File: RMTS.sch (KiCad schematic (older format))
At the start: 68 parts, among them J1 USB_B_Mini, J10 CONN_02, J2 Programmer, J3 Screw_Terminal_01x03, J4 Screw_Terminal_01x04, J5 Screw_Terminal_01x02, J6 Screw_Terminal_01x02, J7 Micro_SD_Card_Det_Hirose_DM3AT, J8 Screw_Terminal_01x02, J9 CONN_02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

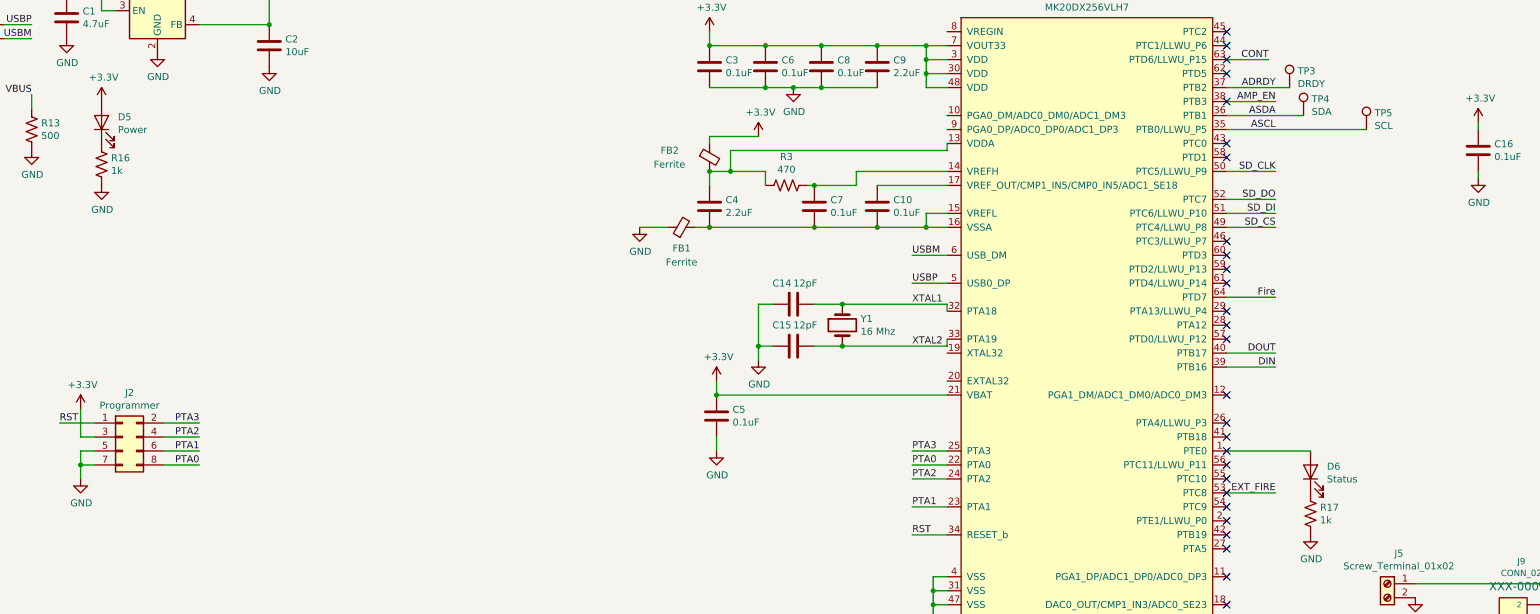
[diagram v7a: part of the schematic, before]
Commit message: Added headers for LEDs, aligned some components better
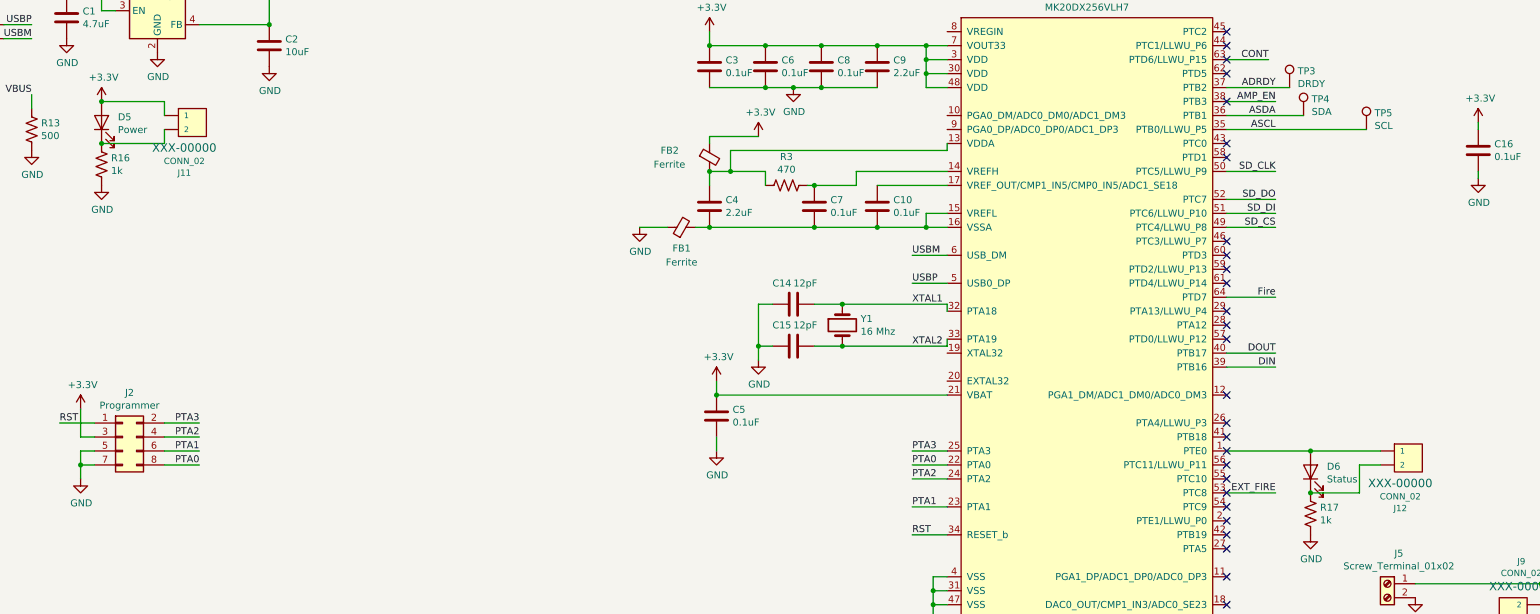
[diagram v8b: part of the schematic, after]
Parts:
- added J11, J12: CONN_02, Connectors:1X02, symbol RMTS-rescue:CONN_02-SparkFun-Connectors-RMTS-rescue
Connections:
- net +3V3: now also J11.1
- net at D6.2 (A), U2.1 (PTE0): now also J12.1
- net at D5.1 (K), R16.1: now also J11.2
- net at D6.1 (K), R17.1: now also J12.2
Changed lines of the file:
@@
 Wire Wire Line
 	10450 4500 11050 4500
+$Comp
+L RMTS-rescue:CONN_02-SparkFun-Connectors-RMTS-rescue J11
+U 1 1 5E6AA3F7
+P 2950 2100
+F 0 "J11" H 2908 2510 45  0000 C CNN
+F 1 "CONN_02" H 2908 2426 45  0000 C CNN
+F 2 "Connectors:1X02" H 2950 2350 20  0001 C CNN
+F 3 "" H 2950 2100 50  0001 C CNN
+F 4 "XXX-00000" H 2908 2331 60  0000 C CNN "Field4"
+	1    2950 2100
+	-1   0    0    1
+$EndComp
+Wire Wire Line
+	2400 2000 2850 2000
+Wire Wire Line
+	2850 2000 2850 2100
+Connection ~ 2400 2000
+Wire Wire Line
+	2400 2300 2850 2300
+Wire Wire Line
+	2850 2300 2850 2200
+Connection ~ 2400 2300
+$Comp
+L RMTS-rescue:CONN_02-SparkFun-Connectors-RMTS-rescue J12
+U 1 1 5E6CC993
+P 11650 4500
+F 0 "J12" H 11608 4910 45  0000 C CNN
+F 1 "CONN_02" H 11608 4826 45  0000 C CNN
+F 2 "Connectors:1X02" H 11650 4750 20  0001 C CNN
+F 3 "" H 11650 4500 50  0001 C CNN
+F 4 "XXX-00000" H 11608 4731 60  0000 C CNN "Field4"
+	1    11650 4500
+	-1   0    0    1
+$EndComp
+Wire Wire Line
+	11050 4500 11550 4500
+Connection ~ 11050 4500
+Wire Wire Line
+	11550 4600 11400 4600
+Wire Wire Line
+	11400 4600 11400 4800
+Wire Wire Line
+	11400 4800 11050 4800
+Connection ~ 11050 4800
 $EndSCHEMATC
